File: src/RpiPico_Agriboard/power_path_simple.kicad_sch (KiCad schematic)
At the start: 7 parts, among them Q12 BSP170P-VB, Q13 BSP170P-VB

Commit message: schematic updates completed
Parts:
- renumbered C30 to C27, C37 to C28, D6 to D12, R24 to R58, R27 to R59
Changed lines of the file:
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@@
       )
       (project "RpiPico_Agriboard"
-        (path "/c2474b65-c0e8-4987-86b2-fddddd4113dc/6578793a-18cf-4100-aa8d-b3f918b44a8b/705d5845-37bb-48c7-9641-198316a19ba9"
-          (reference "Q12") (unit 1)
+        (path "/c2474b65-c0e8-4987-86b2-fddddd4113dc/f3a00526-8108-483c-9ec5-d5fcf6fe065b/e1b77c03-2b38-43f3-998b-3c2f1972d847"
+          (reference "Q?") (unit 1)
         )
       )
@@
   (symbol (lib_id "Device:C_Small") (at 206.375 102.87 0) (unit 1)
     (in_bom yes) (on_board yes) (dnp no)
-    (property "Reference" "C30" (at 208.915 101.6062 0)
+    (property "Reference" "C27" (at 208.915 101.6062 0)
       (effects (font (size 1.27 1.27)) (justify left))
     )
@@
       )
       (project "RpiPico_Agriboard"
-        (path "/c2474b65-c0e8-4987-86b2-fddddd4113dc/6578793a-18cf-4100-aa8d-b3f918b44a8b/705d5845-37bb-48c7-9641-198316a19ba9"
-          (reference "C30") (unit 1)
+        (path "/c2474b65-c0e8-4987-86b2-fddddd4113dc/f3a00526-8108-483c-9ec5-d5fcf6fe065b/e1b77c03-2b38-43f3-998b-3c2f1972d847"
+          (reference "C?") (unit 1)
         )
       )
@@
   (symbol (lib_id "Device:D_Schottky") (at 154.305 116.84 180) (unit 1)
     (in_bom yes) (on_board yes) (dnp no) (fields_autoplaced)
-    (property "Reference" "D6" (at 155.8926 119.38 90)
+    (property "Reference" "D12" (at 155.8926 119.38 90)
       (effects (font (size 1.27 1.27)) (justify left))
     )
@@
       )
       (project "RpiPico_Agriboard"
-        (path "/c2474b65-c0e8-4987-86b2-fddddd4113dc/6578793a-18cf-4100-aa8d-b3f918b44a8b/705d5845-37bb-48c7-9641-198316a19ba9"
-          (reference "D6") (unit 1)
+        (path "/c2474b65-c0e8-4987-86b2-fddddd4113dc/f3a00526-8108-483c-9ec5-d5fcf6fe065b/e1b77c03-2b38-43f3-998b-3c2f1972d847"
+          (reference "D?") (unit 1)
         )
       )
@@
       )
       (project "RpiPico_Agriboard"
-        (path "/c2474b65-c0e8-4987-86b2-fddddd4113dc/6578793a-18cf-4100-aa8d-b3f918b44a8b/705d5845-37bb-48c7-9641-198316a19ba9"
-          (reference "#PWR078") (unit 1)
+        (path "/c2474b65-c0e8-4987-86b2-fddddd4113dc/f3a00526-8108-483c-9ec5-d5fcf6fe065b/e1b77c03-2b38-43f3-998b-3c2f1972d847"
+          (reference "#PWR058") (unit 1)
         )
       )
@@
       )
       (project "RpiPico_Agriboard"
-        (path "/c2474b65-c0e8-4987-86b2-fddddd4113dc/6578793a-18cf-4100-aa8d-b3f918b44a8b/705d5845-37bb-48c7-9641-198316a19ba9"
-          (reference "#PWR080") (unit 1)
+        (path "/c2474b65-c0e8-4987-86b2-fddddd4113dc/f3a00526-8108-483c-9ec5-d5fcf6fe065b/e1b77c03-2b38-43f3-998b-3c2f1972d847"
+          (reference "#PWR060") (unit 1)
         )
       )
@@
   (symbol (lib_id "Device:R_US") (at 134.62 93.98 90) (unit 1)
     (in_bom yes) (on_board yes) (dnp no) (fields_autoplaced)
-    (property "Reference" "R24" (at 134.62 88.265 90)
+    (property "Reference" "R58" (at 134.62 88.265 90)
       (effects (font (size 1.27 1.27)))
     )
@@
       )
       (project "RpiPico_Agriboard"
-        (path "/c2474b65-c0e8-4987-86b2-fddddd4113dc/6578793a-18cf-4100-aa8d-b3f918b44a8b/705d5845-37bb-48c7-9641-198316a19ba9"
-          (reference "R24") (unit 1)
+        (path "/c2474b65-c0e8-4987-86b2-fddddd4113dc/f3a00526-8108-483c-9ec5-d5fcf6fe065b/e1b77c03-2b38-43f3-998b-3c2f1972d847"
+          (reference "R?") (unit 1)
         )
       )
@@
       )
       (project "RpiPico_Agriboard"
-        (path "/c2474b65-c0e8-4987-86b2-fddddd4113dc/6578793a-18cf-4100-aa8d-b3f918b44a8b/705d5845-37bb-48c7-9641-198316a19ba9"
-          (reference "#PWR079") (unit 1)
+        (path "/c2474b65-c0e8-4987-86b2-fddddd4113dc/f3a00526-8108-483c-9ec5-d5fcf6fe065b/e1b77c03-2b38-43f3-998b-3c2f1972d847"
+          (reference "#PWR059") (unit 1)
         )
       )
@@
       )
       (project "RpiPico_Agriboard"
-        (path "/c2474b65-c0e8-4987-86b2-fddddd4113dc/6578793a-18cf-4100-aa8d-b3f918b44a8b/705d5845-37bb-48c7-9641-198316a19ba9"
-          (reference "Q13") (unit 1)
+        (path "/c2474b65-c0e8-4987-86b2-fddddd4113dc/f3a00526-8108-483c-9ec5-d5fcf6fe065b/e1b77c03-2b38-43f3-998b-3c2f1972d847"
+          (reference "Q?") (unit 1)
         )
       )
@@
   (symbol (lib_id "Device:R_US") (at 142.875 99.06 0) (unit 1)
     (in_bom yes) (on_board yes) (dnp no) (fields_autoplaced)
-    (property "Reference" "R27" (at 145.415 97.7899 0)
+    (property "Reference" "R59" (at 145.415 97.7899 0)
       (effects (font (size 1.27 1.27)) (justify left))
     )
@@
       )
       (project "RpiPico_Agriboard"
-        (path "/c2474b65-c0e8-4987-86b2-fddddd4113dc/6578793a-18cf-4100-aa8d-b3f918b44a8b/705d5845-37bb-48c7-9641-198316a19ba9"
-          (reference "R27") (unit 1)
+        (path "/c2474b65-c0e8-4987-86b2-fddddd4113dc/f3a00526-8108-483c-9ec5-d5fcf6fe065b/e1b77c03-2b38-43f3-998b-3c2f1972d847"
+          (reference "R?") (unit 1)
         )
       )
@@
   (symbol (lib_id "Device:C_Small") (at 215.265 102.87 0) (unit 1)
     (in_bom yes) (on_board yes) (dnp no)
-    (property "Reference" "C37" (at 217.805 101.6062 0)
+    (property "Reference" "C28" (at 217.805 101.6062 0)
       (effects (font (size 1.27 1.27)) (justify left))
     )
@@
       )
       (project "RpiPico_Agriboard"
-        (path "/c2474b65-c0e8-4987-86b2-fddddd4113dc/6578793a-18cf-4100-aa8d-b3f918b44a8b/705d5845-37bb-48c7-9641-198316a19ba9"
-          (reference "C37") (unit 1)
-        )
-      )
+        (path "/c2474b65-c0e8-4987-86b2-fddddd4113dc/f3a00526-8108-483c-9ec5-d5fcf6fe065b/e1b77c03-2b38-43f3-998b-3c2f1972d847"
+          (reference "C?") (unit 1)
+        )
+      )

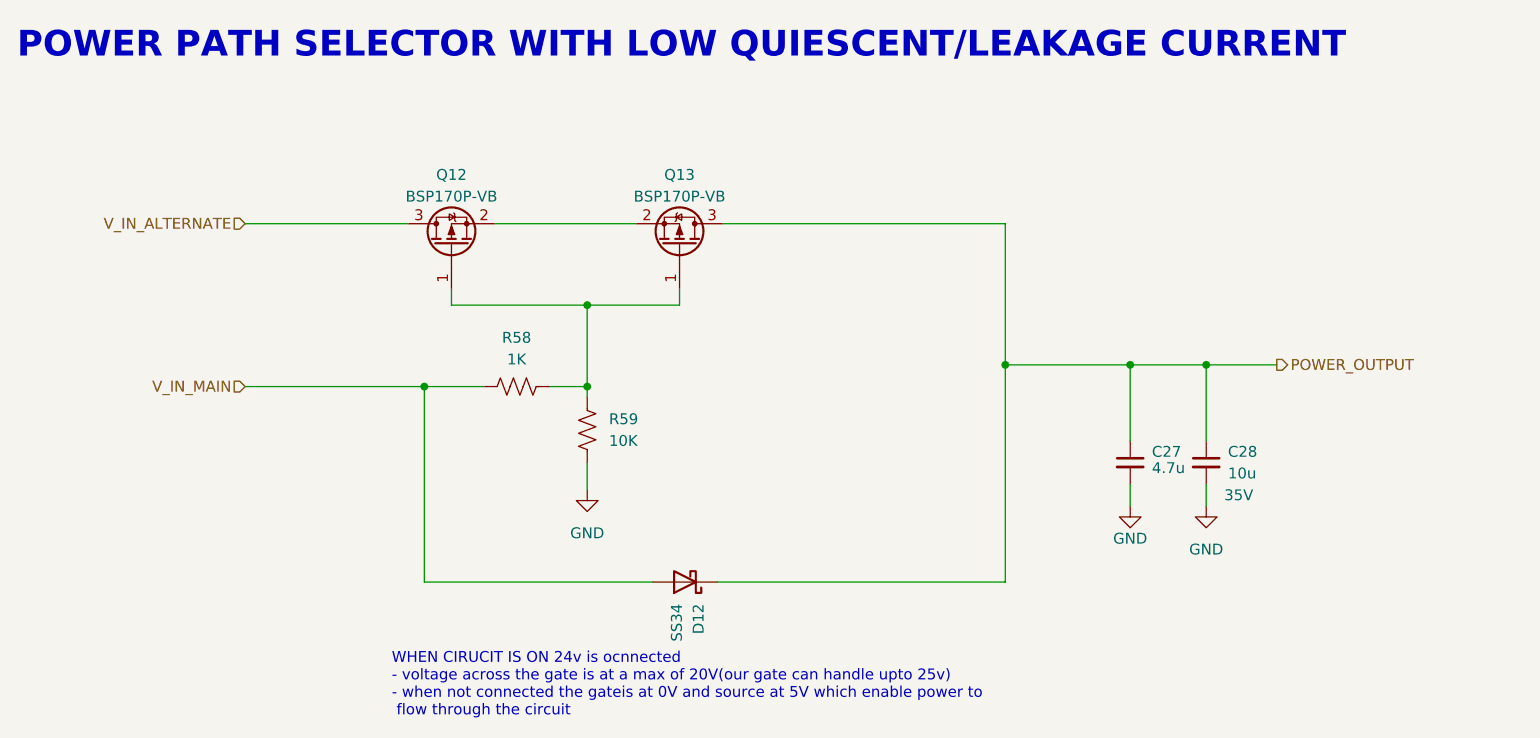
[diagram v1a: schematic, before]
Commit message: Revert "schematic updates completed"
This reverts commit 0124993096667d53f20fd59dec80d3f5a1efcd43.
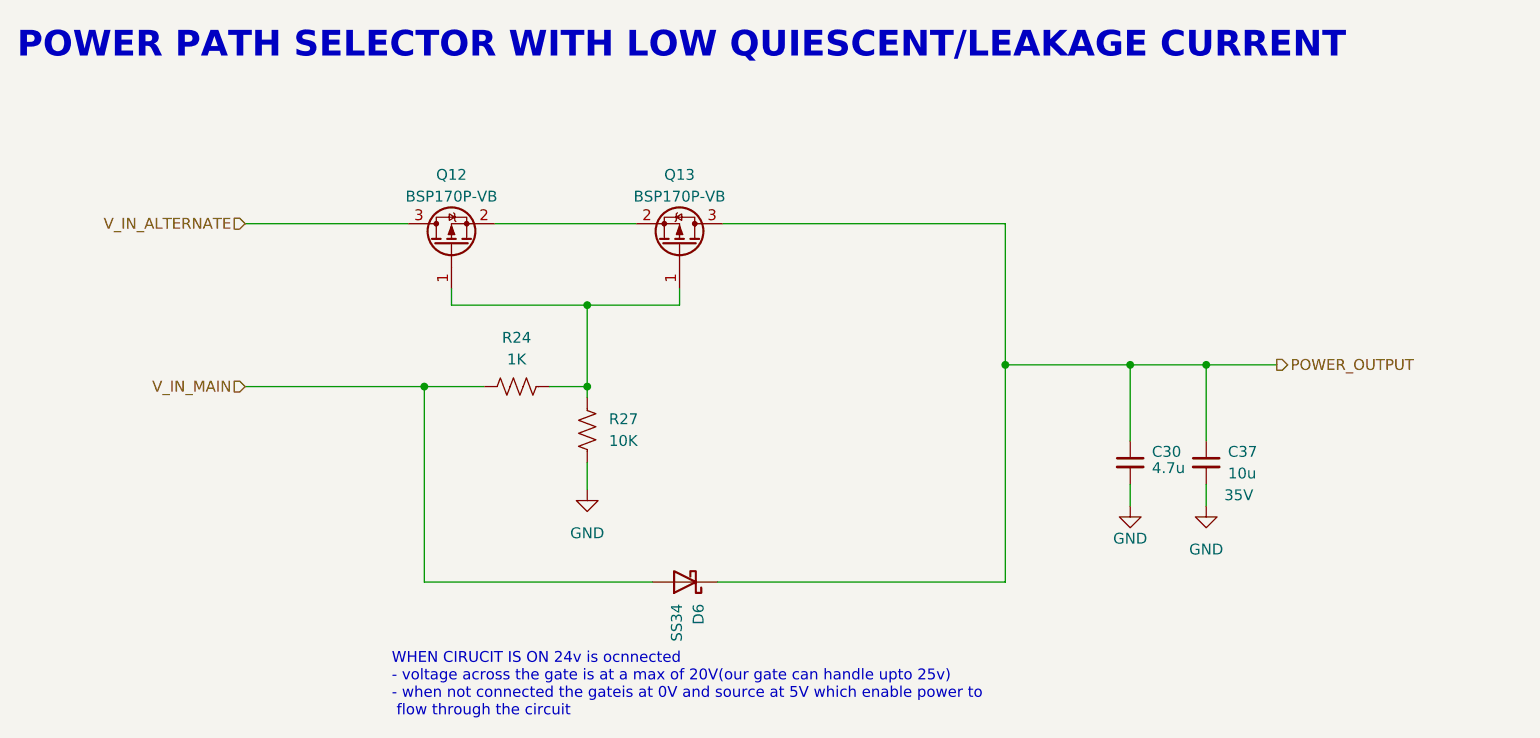
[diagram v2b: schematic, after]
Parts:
- renumbered C27 to C30, C28 to C37, D12 to D6, R58 to R24, R59 to R27
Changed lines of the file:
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@@
       )
       (project "RpiPico_Agriboard"
-        (path "/c2474b65-c0e8-4987-86b2-fddddd4113dc/f3a00526-8108-483c-9ec5-d5fcf6fe065b/e1b77c03-2b38-43f3-998b-3c2f1972d847"
-          (reference "Q?") (unit 1)
+        (path "/c2474b65-c0e8-4987-86b2-fddddd4113dc/6578793a-18cf-4100-aa8d-b3f918b44a8b/705d5845-37bb-48c7-9641-198316a19ba9"
+          (reference "Q12") (unit 1)
         )
       )
@@
   (symbol (lib_id "Device:C_Small") (at 206.375 102.87 0) (unit 1)
     (in_bom yes) (on_board yes) (dnp no)
-    (property "Reference" "C27" (at 208.915 101.6062 0)
+    (property "Reference" "C30" (at 208.915 101.6062 0)
       (effects (font (size 1.27 1.27)) (justify left))
     )
@@
       )
       (project "RpiPico_Agriboard"
-        (path "/c2474b65-c0e8-4987-86b2-fddddd4113dc/f3a00526-8108-483c-9ec5-d5fcf6fe065b/e1b77c03-2b38-43f3-998b-3c2f1972d847"
-          (reference "C?") (unit 1)
+        (path "/c2474b65-c0e8-4987-86b2-fddddd4113dc/6578793a-18cf-4100-aa8d-b3f918b44a8b/705d5845-37bb-48c7-9641-198316a19ba9"
+          (reference "C30") (unit 1)
         )
       )
@@
   (symbol (lib_id "Device:D_Schottky") (at 154.305 116.84 180) (unit 1)
     (in_bom yes) (on_board yes) (dnp no) (fields_autoplaced)
-    (property "Reference" "D12" (at 155.8926 119.38 90)
+    (property "Reference" "D6" (at 155.8926 119.38 90)
       (effects (font (size 1.27 1.27)) (justify left))
     )
@@
       )
       (project "RpiPico_Agriboard"
-        (path "/c2474b65-c0e8-4987-86b2-fddddd4113dc/f3a00526-8108-483c-9ec5-d5fcf6fe065b/e1b77c03-2b38-43f3-998b-3c2f1972d847"
-          (reference "D?") (unit 1)
+        (path "/c2474b65-c0e8-4987-86b2-fddddd4113dc/6578793a-18cf-4100-aa8d-b3f918b44a8b/705d5845-37bb-48c7-9641-198316a19ba9"
+          (reference "D6") (unit 1)
         )
       )
@@
       )
       (project "RpiPico_Agriboard"
-        (path "/c2474b65-c0e8-4987-86b2-fddddd4113dc/f3a00526-8108-483c-9ec5-d5fcf6fe065b/e1b77c03-2b38-43f3-998b-3c2f1972d847"
-          (reference "#PWR058") (unit 1)
+        (path "/c2474b65-c0e8-4987-86b2-fddddd4113dc/6578793a-18cf-4100-aa8d-b3f918b44a8b/705d5845-37bb-48c7-9641-198316a19ba9"
+          (reference "#PWR078") (unit 1)
         )
       )
@@
       )
       (project "RpiPico_Agriboard"
-        (path "/c2474b65-c0e8-4987-86b2-fddddd4113dc/f3a00526-8108-483c-9ec5-d5fcf6fe065b/e1b77c03-2b38-43f3-998b-3c2f1972d847"
-          (reference "#PWR060") (unit 1)
+        (path "/c2474b65-c0e8-4987-86b2-fddddd4113dc/6578793a-18cf-4100-aa8d-b3f918b44a8b/705d5845-37bb-48c7-9641-198316a19ba9"
+          (reference "#PWR080") (unit 1)
         )
       )
@@
   (symbol (lib_id "Device:R_US") (at 134.62 93.98 90) (unit 1)
     (in_bom yes) (on_board yes) (dnp no) (fields_autoplaced)
-    (property "Reference" "R58" (at 134.62 88.265 90)
+    (property "Reference" "R24" (at 134.62 88.265 90)
       (effects (font (size 1.27 1.27)))
     )
@@
       )
       (project "RpiPico_Agriboard"
-        (path "/c2474b65-c0e8-4987-86b2-fddddd4113dc/f3a00526-8108-483c-9ec5-d5fcf6fe065b/e1b77c03-2b38-43f3-998b-3c2f1972d847"
-          (reference "R?") (unit 1)
+        (path "/c2474b65-c0e8-4987-86b2-fddddd4113dc/6578793a-18cf-4100-aa8d-b3f918b44a8b/705d5845-37bb-48c7-9641-198316a19ba9"
+          (reference "R24") (unit 1)
         )
       )
@@
       )
       (project "RpiPico_Agriboard"
-        (path "/c2474b65-c0e8-4987-86b2-fddddd4113dc/f3a00526-8108-483c-9ec5-d5fcf6fe065b/e1b77c03-2b38-43f3-998b-3c2f1972d847"
-          (reference "#PWR059") (unit 1)
+        (path "/c2474b65-c0e8-4987-86b2-fddddd4113dc/6578793a-18cf-4100-aa8d-b3f918b44a8b/705d5845-37bb-48c7-9641-198316a19ba9"
+          (reference "#PWR079") (unit 1)
         )
       )
@@
       )
       (project "RpiPico_Agriboard"
-        (path "/c2474b65-c0e8-4987-86b2-fddddd4113dc/f3a00526-8108-483c-9ec5-d5fcf6fe065b/e1b77c03-2b38-43f3-998b-3c2f1972d847"
-          (reference "Q?") (unit 1)
+        (path "/c2474b65-c0e8-4987-86b2-fddddd4113dc/6578793a-18cf-4100-aa8d-b3f918b44a8b/705d5845-37bb-48c7-9641-198316a19ba9"
+          (reference "Q13") (unit 1)
         )
       )
@@
   (symbol (lib_id "Device:R_US") (at 142.875 99.06 0) (unit 1)
     (in_bom yes) (on_board yes) (dnp no) (fields_autoplaced)
-    (property "Reference" "R59" (at 145.415 97.7899 0)
+    (property "Reference" "R27" (at 145.415 97.7899 0)
       (effects (font (size 1.27 1.27)) (justify left))
     )
@@
       )
       (project "RpiPico_Agriboard"
-        (path "/c2474b65-c0e8-4987-86b2-fddddd4113dc/f3a00526-8108-483c-9ec5-d5fcf6fe065b/e1b77c03-2b38-43f3-998b-3c2f1972d847"
-          (reference "R?") (unit 1)
+        (path "/c2474b65-c0e8-4987-86b2-fddddd4113dc/6578793a-18cf-4100-aa8d-b3f918b44a8b/705d5845-37bb-48c7-9641-198316a19ba9"
+          (reference "R27") (unit 1)
         )
       )
@@
   (symbol (lib_id "Device:C_Small") (at 215.265 102.87 0) (unit 1)
     (in_bom yes) (on_board yes) (dnp no)
-    (property "Reference" "C28" (at 217.805 101.6062 0)
+    (property "Reference" "C37" (at 217.805 101.6062 0)
       (effects (font (size 1.27 1.27)) (justify left))
     )
@@
       )
       (project "RpiPico_Agriboard"
-        (path "/c2474b65-c0e8-4987-86b2-fddddd4113dc/f3a00526-8108-483c-9ec5-d5fcf6fe065b/e1b77c03-2b38-43f3-998b-3c2f1972d847"
-          (reference "C?") (unit 1)
-        )
-      )
+        (path "/c2474b65-c0e8-4987-86b2-fddddd4113dc/6578793a-18cf-4100-aa8d-b3f918b44a8b/705d5845-37bb-48c7-9641-198316a19ba9"
+          (reference "C37") (unit 1)
+        )
+      )
